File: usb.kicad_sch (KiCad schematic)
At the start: 47 parts, among them Q1 PJE138K, Q4 PJE138K, U1 MPFS250T-FCVG484, U13 USB3315-CP-TR, U22 PI3USB102GZLEX, U23 PI3USB102GZLEX, U28 USB2422-I/MJ, Y1 Oscillator_24MHz_ESC_2016MV

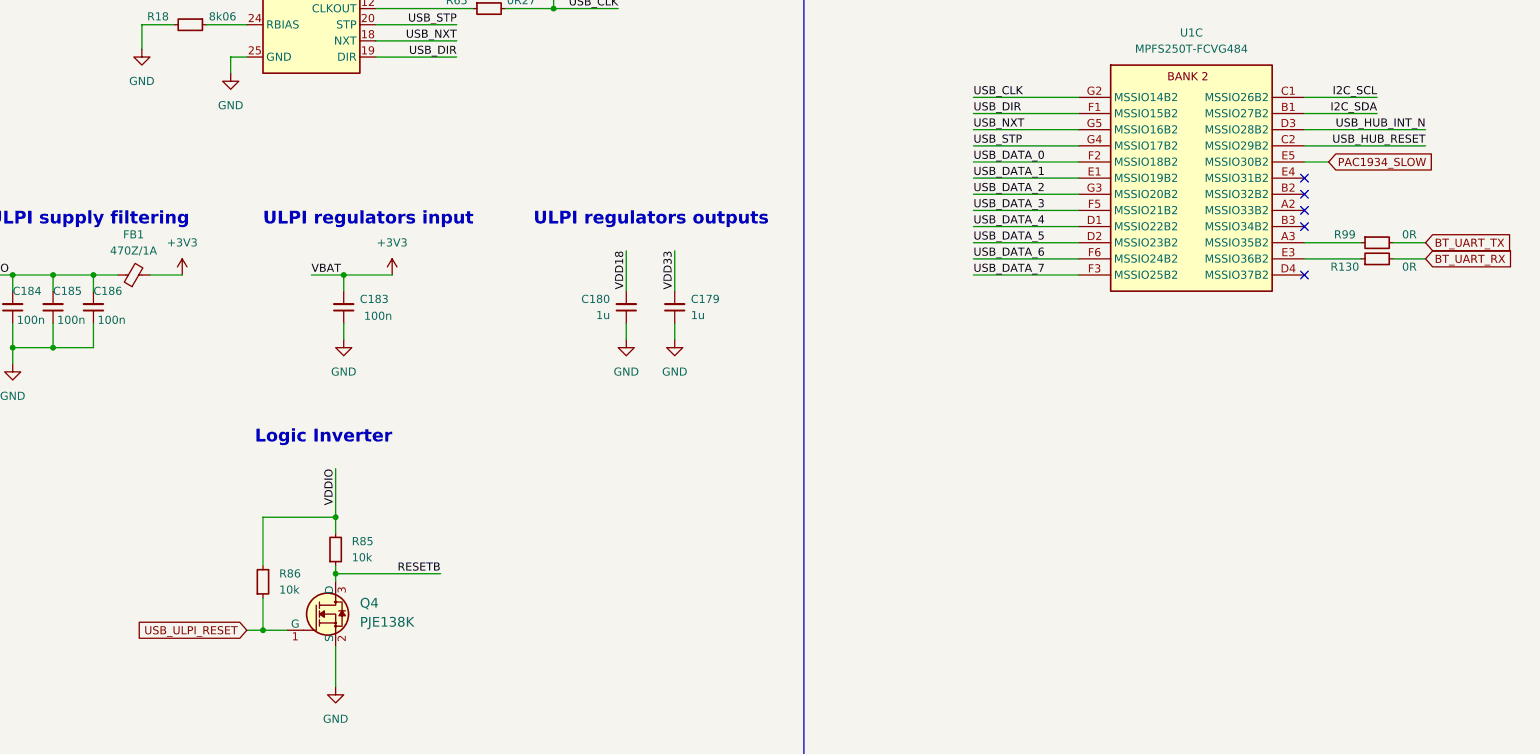
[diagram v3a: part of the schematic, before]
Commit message: [#56715] Change resistor size, USB VDDIO and reset
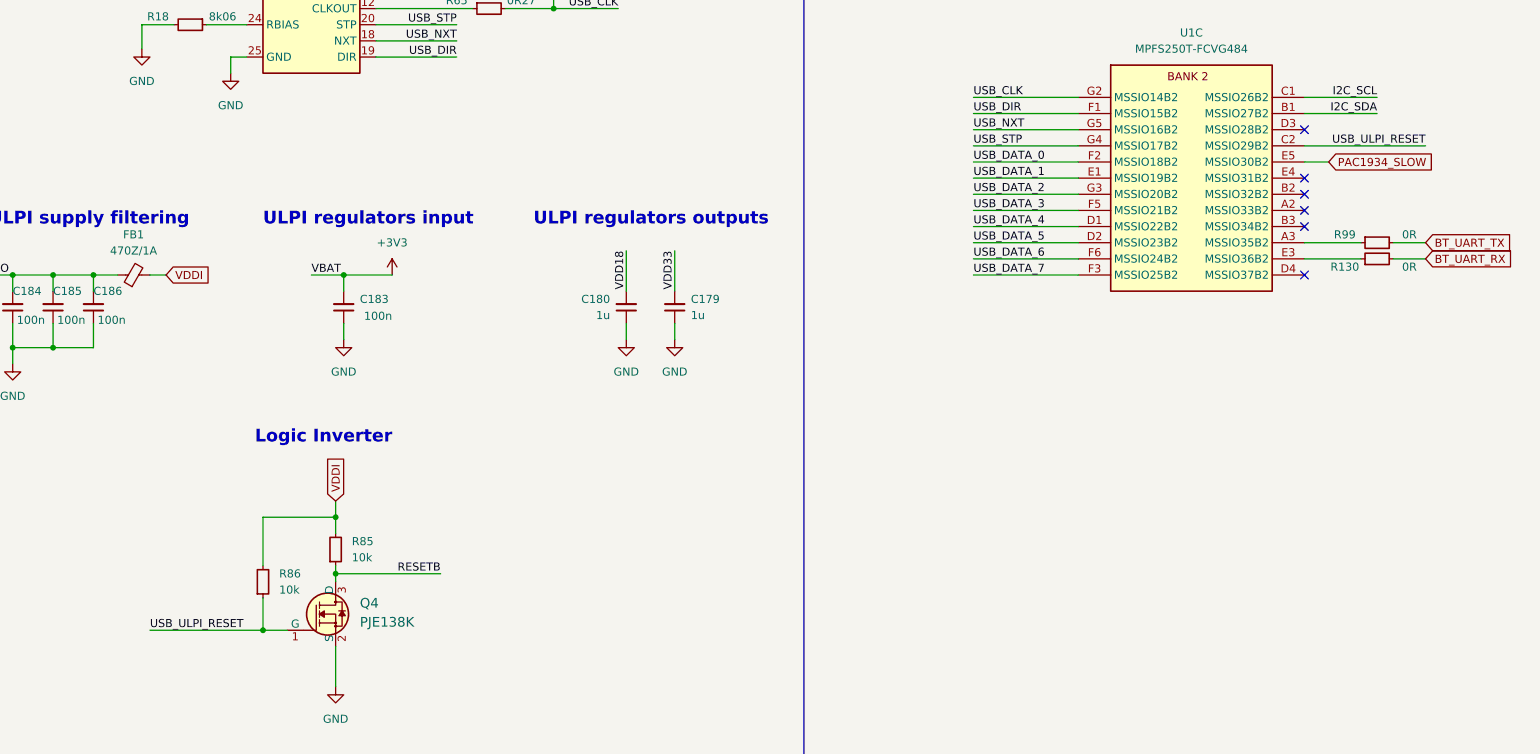
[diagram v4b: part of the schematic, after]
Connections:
- net USB_HUB_RESET is gone; now on net USB_ULPI_RESET: U1.C2 (MSSIO29B2)
- net +3V3: no longer FB1.2
- net VDDI: now also FB1.2, R85.2, R86.2
- net VDDIO: no longer R85.2, R86.2
- net USB_HUB_INT_N: no longer names the net of U1.D3 (MSSIO28B2)
- no-connect marks 10 -> 11
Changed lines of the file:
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@@
   (junction (at 62.23 63.5) (diameter 0) (color 0 0 0 0)
   )
-  (junction (at 215.9 236.22) (diameter 0) (color 0 0 0 0)
-  )
   (junction (at 204.47 254) (diameter 0) (color 0 0 0 0)
   )
@@
   (junction (at 217.17 198.12) (diameter 0) (color 0 0 0 0)
   )
+  (junction (at 215.9 236.22) (diameter 0) (color 0 0 0 0)
+  )
   (junction (at 250.19 156.21) (diameter 0) (color 0 0 0 0)
   )
@@
   )
   (no_connect (at 92.71 132.08))
+  (no_connect (at 368.3 175.26))
   (no_connect (at 368.3 198.12))
   (no_connect (at 59.69 152.4))
@@
     (stroke (width 0) (type default))
   )
-  (wire (pts (xy 191.77 198.12) (xy 186.69 198.12))
+  (wire (pts (xy 189.23 198.12) (xy 186.69 198.12))
     (stroke (width 0) (type default))
   )
@@
     (stroke (width 0) (type default))
   )
+  (wire (pts (xy 204.47 236.22) (xy 215.9 236.22))
+    (stroke (width 0) (type default))
+  )
   (wire (pts (xy 64.77 219.71) (xy 53.34 219.71))
     (stroke (width 0) (type default))
@@
     (stroke (width 0) (type default))
   )
-  (wire (pts (xy 368.3 175.26) (xy 387.35 175.26))
-    (stroke (width 0) (type default))
-  )
   (wire (pts (xy 62.23 55.88) (xy 71.12 55.88))
     (stroke (width 0) (type default))
@@
     (stroke (width 0) (type default))
   )
-  (wire (pts (xy 215.9 228.6) (xy 215.9 236.22))
-    (stroke (width 0) (type default))
-  )
   (wire (pts (xy 125.73 139.7) (xy 134.62 139.7))
     (stroke (width 0) (type default))
@@
     (stroke (width 0) (type default))
   )
-  (wire (pts (xy 201.93 254) (xy 204.47 254))
+  (wire (pts (xy 186.69 254) (xy 204.47 254))
     (stroke (width 0) (type default))
   )
@@
     (stroke (width 0) (type default))
   )
-  (wire (pts (xy 215.9 236.22) (xy 215.9 238.76))
-    (stroke (width 0) (type default))
-  )
   (wire (pts (xy 165.1 198.12) (xy 171.45 198.12))
     (stroke (width 0) (type default))
@@
     (stroke (width 0) (type default))
   )
-  (wire (pts (xy 204.47 236.22) (xy 215.9 236.22))
-    (stroke (width 0) (type default))
-  )
   (wire (pts (xy 92.71 138.43) (xy 105.41 138.43))
     (stroke (width 0) (type default))
@@
     (stroke (width 0) (type default))
   )
+  (wire (pts (xy 215.9 233.68) (xy 215.9 236.22))
+    (stroke (width 0) (type default))
+  )
   (wire (pts (xy 316.23 187.96) (xy 332.74 187.96))
     (stroke (width 0) (type default))
@@
     (stroke (width 0) (type default))
   )
+  (wire (pts (xy 215.9 236.22) (xy 215.9 238.76))
+    (stroke (width 0) (type default))
+  )
   (wire (pts (xy 62.23 63.5) (xy 71.12 63.5))
     (stroke (width 0) (type default))
@@
     (effects (font (size 1.27 1.27)) (justify right bottom))
   )
-  (label "USB_HUB_RESET" (at 387.35 177.8 180) (fields_autoplaced)
-    (effects (font (size 1.27 1.27)) (justify right bottom))
-  )
   (label "I2C_SCL" (at 379.73 170.18 180) (fields_autoplaced)
     (effects (font (size 1.27 1.27)) (justify right bottom))
@@
     (effects (font (size 1.27 1.27)) (justify left bottom))
   )
-  (label "VDDIO" (at 215.9 228.6 270) (fields_autoplaced)
-    (effects (font (size 1.27 1.27)) (justify right bottom))
+  (label "USB_ULPI_RESET" (at 186.69 254 0) (fields_autoplaced)
+    (effects (font (size 1.27 1.27)) (justify left bottom))
   )
   (label "~{BYP_EN}" (at 219.71 54.61 0) (fields_autoplaced)
@@
     (effects (font (size 1.27 1.27)) (justify right bottom))
   )
-  (label "USB_HUB_INT_N" (at 387.35 175.26 180) (fields_autoplaced)
-    (effects (font (size 1.27 1.27)) (justify right bottom))
-  )
   (label "USB_NXT" (at 234.95 161.29 180) (fields_autoplaced)
     (effects (font (size 1.27 1.27)) (justify right bottom))
@@
     (effects (font (size 1.27 1.27)) (justify left bottom))
   )
+  (label "USB_ULPI_RESET" (at 387.35 177.8 180) (fields_autoplaced)
+    (effects (font (size 1.27 1.27)) (justify right bottom))
+  )
   (label "VDD18" (at 229.87 130.81 180) (fields_autoplaced)
     (effects (font (size 1.27 1.27)) (justify right bottom))
@@
     )
   )
+  (global_label "VDDI" (shape input) (at 189.23 198.12 0) (fields_autoplaced)
+    (effects (font (size 1.27 1.27)) (justify left))
+    (property "Intersheetrefs" "${INTERSHEET_REFS}" (at 196.4486 198.12 0)
+      (effects (font (size 1.27 1.27)) (justify left) hide)
+    )
+  )
   (global_label "PMIC_SDA" (shape bidirectional) (at 350.52 53.34 0) (fields_autoplaced)
     (effects (font (size 1.27 1.27)) (justify left))
@@
     )
   )
+  (global_label "VDDI" (shape input) (at 215.9 233.68 90) (fields_autoplaced)
+    (effects (font (size 1.27 1.27)) (justify left))
+    (property "Intersheetrefs" "${INTERSHEET_REFS}" (at 215.9 226.4614 90)
+      (effects (font (size 1.27 1.27)) (justify left) hide)
+    )
+  )
   (global_label "CONN_USB_N" (shape input) (at 127 215.9 0) (fields_autoplaced)
     (effects (font (size 1.27 1.27)) (justify left))
@@
     )
   )
-  (global_label "USB_ULPI_RESET" (shape input) (at 201.93 254 180) (fields_autoplaced)
-    (effects (font (size 1.27 1.27)) (justify right))
-    (property "Intersheetrefs" "${INTERSHEET_REFS}" (at 183.7931 253.9206 0)
-      (effects (font (size 1.27 1.27)) (justify right) hide)
-    )
-  )
   (global_label "PAC1934_SCL" (shape output) (at 350.52 59.69 0) (fields_autoplaced)
     (effects (font (size 1.27 1.27)) (justify left))
@@
         )
       )
-    )
-  )
-  (symbol (lib_id "antmicropower:+3V3") (at 191.77 198.12 0) (unit 1)
-    (in_bom yes) (on_board yes) (dnp no)
-    (property "Reference" "#PWR0166" (at 207.01 200.66 0)
-      (effects (font (size 1.27 1.27) (thickness 0.15)) (justify left bottom) hide)
-    )
-    (property "Value" "+3V3" (at 191.77 193.04 0)
-      (effects (font (size 1.27 1.27) (thickness 0.15)))
-    )
-    (property "Footprint" "" (at 207.01 205.74 0)
-      (effects (font (size 1.27 1.27) (thickness 0.15)) (justify left bottom) hide)
-    )
-    (property "Datasheet" "" (at 207.01 208.28 0)
-      (effects (font (size 1.27 1.27) (thickness 0.15)) (justify left bottom) hide)
-    )
-    (property "Author" "Antmicro" (at 207.01 205.74 0)
-      (effects (font (size 1.27 1.27) (thickness 0.15)) (justify left bottom) hide)
-    )
-    (property "License" "Apache-2.0" (at 207.01 208.28 0)
-      (effects (font (size 1.27 1.27) (thickness 0.15)) (justify left bottom) hide)
-    )
-    (pin "1")
-    (instances
-      (project "polarfire-som"
-        (path "/db4a0d3e-2eb3-499e-977d-6eb378cfd3ed/d93d65d4-e21e-44e3-82fb-4ad52468a6b3"
-          (reference "#PWR0166") (unit 1)
-        )
-      )

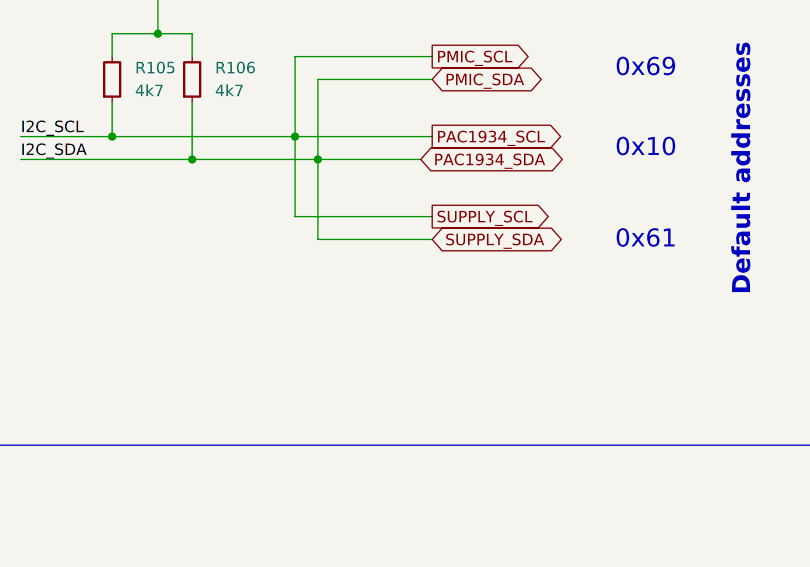
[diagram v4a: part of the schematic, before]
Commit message: [#56715] Improve HDMI0, add ID_SC and ID_SD connections
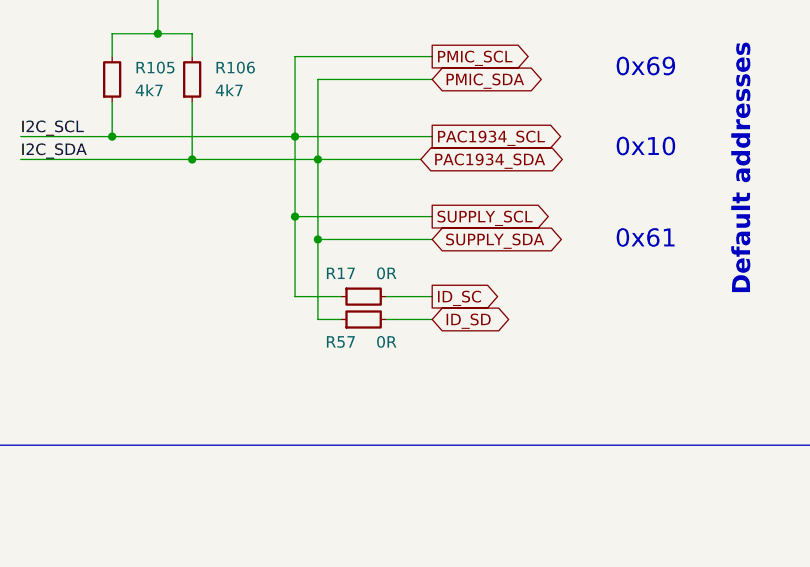
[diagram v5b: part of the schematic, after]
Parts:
- added R17, R57: R_0R_0402, antmicro-footprints:R_0402_1005Metric, symbol antmicroResistors0402:R_0R_0402
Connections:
- net PAC1934_SCL: now also R17.1
- net PAC1934_SDA: now also R57.1
- new net ID_SC: R17.2
- new net ID_SD: R57.2
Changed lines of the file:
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@@
     (comment 1 "www.antmicro.com")
   )
+  (junction (at 337.82 71.12) (diameter 0) (color 0 0 0 0)
+  )
   (junction (at 191.77 139.7) (diameter 0) (color 0 0 0 0)
   )
@@
   (junction (at 46.99 172.72) (diameter 0) (color 0 0 0 0)
   )
+  (junction (at 335.28 68.58) (diameter 0) (color 0 0 0 0)
+  )
   (junction (at 62.23 63.5) (diameter 0) (color 0 0 0 0)
   )
@@
     (stroke (width 0) (type default))
   )
+  (wire (pts (xy 345.44 80.01) (xy 350.52 80.01))
+    (stroke (width 0) (type default))
+  )
   (wire (pts (xy 101.6 224.79) (xy 111.76 224.79))
     (stroke (width 0) (type default))
@@
     (stroke (width 0) (type default))
   )
+  (wire (pts (xy 337.82 80.01) (xy 337.82 71.12))
+    (stroke (width 0) (type default))
+  )
   (wire (pts (xy 124.46 226.06) (xy 124.46 227.33))
     (stroke (width 0) (type default))
@@
     (stroke (width 0) (type default))
   )
+  (wire (pts (xy 340.36 77.47) (xy 335.28 77.47))
+    (stroke (width 0) (type default))
+  )
   (wire (pts (xy 124.46 215.9) (xy 127 215.9))
     (stroke (width 0) (type default))
@@
     (stroke (width 0) (type default))
   )
+  (wire (pts (xy 345.44 77.47) (xy 350.52 77.47))
+    (stroke (width 0) (type default))
+  )
   (wire (pts (xy 222.25 158.75) (xy 234.95 158.75))
     (stroke (width 0) (type default))
@@
     (stroke (width 0) (type default))
   )
+  (wire (pts (xy 340.36 80.01) (xy 337.82 80.01))
+    (stroke (width 0) (type default))
+  )
   (wire (pts (xy 119.38 226.06) (xy 119.38 227.33))
     (stroke (width 0) (type default))
@@
     (stroke (width 0) (type default))
   )
+  (wire (pts (xy 335.28 77.47) (xy 335.28 68.58))
+    (stroke (width 0) (type default))
+  )
   (wire (pts (xy 199.39 64.77) (xy 199.39 67.31))
     (stroke (width 0) (type default))
@@
     )
   )
+  (global_label "ID_SD" (shape bidirectional) (at 350.52 80.01 0) (fields_autoplaced)
+    (effects (font (size 1.27 1.27)) (justify left))
+    (property "Intersheetrefs" "${INTERSHEET_REFS}" (at 359.9384 80.01 0)
+      (effects (font (size 1.27 1.27)) (justify left) hide)
+    )
+  )
   (global_label "CONN_USB_P" (shape input) (at 127 218.44 0) (fields_autoplaced)
     (effects (font (size 1.27 1.27)) (justify left))
@@
     )
   )
+  (global_label "ID_SC" (shape output) (at 350.52 77.47 0) (fields_autoplaced)
+    (effects (font (size 1.27 1.27)) (justify left))
+    (property "Intersheetrefs" "${INTERSHEET_REFS}" (at 358.8271 77.47 0)
+      (effects (font (size 1.27 1.27)) (justify left) hide)
+    )
+  )
   (global_label "WL_BT_USB_P" (shape bidirectional) (at 97.79 149.86 0) (fields_autoplaced)
     (effects (font (size 1.27 1.27)) (justify left))
@@
     )
   )
+  (symbol (lib_id "antmicroResistors0402:R_0R_0402") (at 340.36 80.01 0) (mirror x) (unit 1)
+    (in_bom yes) (on_board yes) (dnp no)
+    (property "Reference" "R57" (at 340.36 82.55 0)
+      (effects (font (size 1.27 1.27) (thickness 0.15)))
+    )
+    (property "Value" "R_0R_0402" (at 360.68 67.31 0)
+      (effects (font (size 1.27 1.27) (thickness 0.15)) (justify left bottom) hide)
+    )
+    (property "Footprint" "antmicro-footprints:R_0402_1005Metric" (at 360.68 64.77 0)
+      (effects (font (size 1.27 1.27) (thickness 0.15)) (justify left bottom) hide)
+    )
+    (property "Datasheet" "https://industrial.panasonic.com/cdbs/www-data/pdf/RDA0000/AOA0000C301.pdf" (at 360.68 62.23 0)
+      (effects (font (size 1.27 1.27) (thickness 0.15)) (justify left bottom) hide)
+    )
+    (property "MPN" "ERJ2GE0R00X" (at 360.68 59.69 0)
+      (effects (font (size 1.27 1.27) (thickness 0.15)) (justify left bottom) hide)
+    )
+    (property "Manufacturer" "Panasonic" (at 360.68 57.15 0)
+      (effects (font (size 1.27 1.27) (thickness 0.15)) (justify left bottom) hide)
+    )
+    (property "License" "Apache-2.0" (at 360.68 54.61 0)
+      (effects (font (size 1.27 1.27) (thickness 0.15)) (justify left bottom) hide)
+    )
+    (property "Author" "Antmicro" (at 360.68 52.07 0)
+      (effects (font (size 1.27 1.27) (thickness 0.15)) (justify left bottom) hide)
+    )
+    (property "Val" "0R" (at 345.44 82.55 0)
+      (effects (font (size 1.27 1.27) (thickness 0.15)))
+    )
+    (property "Tolerance" "~" (at 360.68 69.85 0)
+      (effects (font (size 1.27 1.27)) (justify left bottom) hide)
+    )
+    (property "Current" "1A" (at 360.68 49.53 0)
+      (effects (font (size 1.27 1.27) (thickness 0.15)) (justify left bottom) hide)
+    )
+    (pin "1")
+    (pin "2")
+    (instances
+      (project "polarfire-som"
+        (path "/db4a0d3e-2eb3-499e-977d-6eb378cfd3ed/d93d65d4-e21e-44e3-82fb-4ad52468a6b3"
+          (reference "R57") (unit 1)
+        )
+      )
+    )
+  )
   (symbol (lib_id "antmicroCapacitors0402:C_100n_0402") (at 105.41 170.18 90) (unit 1)
     (in_bom yes) (on_board yes) (dnp no)
@@
         )
       )
+    )
+  )
+  (symbol (lib_id "antmicroResistors0402:R_0R_0402") (at 340.36 77.47 0) (unit 1)
+    (in_bom yes) (on_board yes) (dnp no)
+    (property "Reference" "R17" (at 340.36 74.93 0)
+      (effects (font (size 1.27 1.27) (thickness 0.15)))
+    )
+    (property "Value" "R_0R_0402" (at 360.68 90.17 0)
+      (effects (font (size 1.27 1.27) (thickness 0.15)) (justify left bottom) hide)
+    )
+    (property "Footprint" "antmicro-footprints:R_0402_1005Metric" (at 360.68 92.71 0)
+      (effects (font (size 1.27 1.27) (thickness 0.15)) (justify left bottom) hide)
+    )
+    (property "Datasheet" "https://industrial.panasonic.com/cdbs/www-data/pdf/RDA0000/AOA0000C301.pdf" (at 360.68 95.25 0)
+      (effects (font (size 1.27 1.27) (thickness 0.15)) (justify left bottom) hide)
+    )
+    (property "MPN" "ERJ2GE0R00X" (at 360.68 97.79 0)
+      (effects (font (size 1.27 1.27) (thickness 0.15)) (justify left bottom) hide)
+    )
+    (property "Manufacturer" "Panasonic" (at 360.68 100.33 0)
+      (effects (font (size 1.27 1.27) (thickness 0.15)) (justify left bottom) hide)
+    )
+    (property "License" "Apache-2.0" (at 360.68 102.87 0)
+      (effects (font (size 1.27 1.27) (thickness 0.15)) (justify left bottom) hide)
+    )
+    (property "Author" "Antmicro" (at 360.68 105.41 0)
+      (effects (font (size 1.27 1.27) (thickness 0.15)) (justify left bottom) hide)
+    )
+    (property "Val" "0R" (at 345.44 74.93 0)
+      (effects (font (size 1.27 1.27) (thickness 0.15)))
+    )
+    (property "Tolerance" "~" (at 360.68 87.63 0)
+      (effects (font (size 1.27 1.27)) (justify left bottom) hide)
+    )
+    (property "Current" "1A" (at 360.68 107.95 0)
+      (effects (font (size 1.27 1.27) (thickness 0.15)) (justify left bottom) hide)
+    )
+    (pin "1")
+    (pin "2")
+    (instances
+      (project "polarfire-som"
+        (path "/db4a0d3e-2eb3-499e-977d-6eb378cfd3ed/d93d65d4-e21e-44e3-82fb-4ad52468a6b3"
+          (reference "R17") (unit 1)
+        )
+      )
